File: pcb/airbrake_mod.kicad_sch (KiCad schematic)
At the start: 3 parts

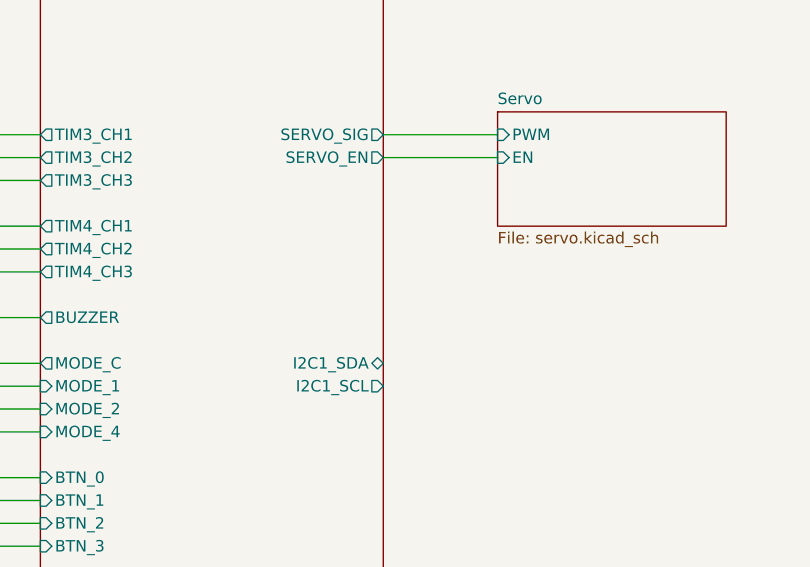
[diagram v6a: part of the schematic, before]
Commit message: Incorporate feedback servo with 4 pin molex and additional ADC channel
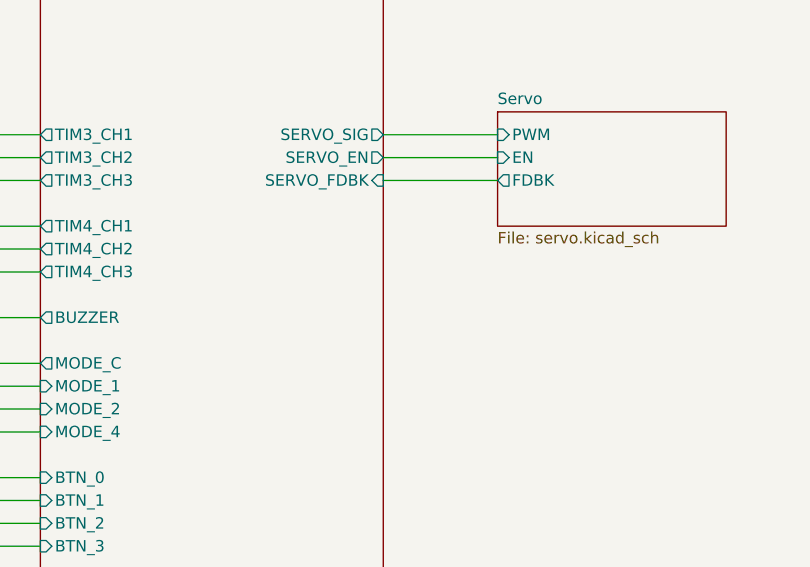
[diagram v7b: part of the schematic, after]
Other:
- sheet MCU ports: added SERVO_FDBK; removed I2C1_SCL, I2C1_SDA
- sheet Servo ports: added FDBK; removed none
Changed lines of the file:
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@@
+	(wire
+		(pts
+			(xy 101.6 121.92) (xy 114.3 121.92)
+		)
+		(stroke
+			(width 0)
+			(type default)
+		)
+	)
 	(wire
 		(pts
@@
 			)
 		)
-		(pin "I2C1_SDA" bidirectional
-			(at 101.6 142.24 0)
-			(effects
-				(font
-					(size 1.27 1.27)
-				)
-				(justify right)
-			)
-		)
-		(pin "I2C1_SCL" output
-			(at 101.6 144.78 0)
-			(effects
-				(font
-					(size 1.27 1.27)
-				)
-				(justify right)
-			)
-		)
 		(pin "USB_D-" bidirectional
 			(at 63.5 30.48 180)
@@
 				)
 				(justify left)
+			)
+		)
+		(pin "SERVO_FDBK" input
+			(at 101.6 121.92 0)
+			(effects
+				(font
+					(size 1.27 1.27)
+				)
+				(justify right)
 			)
 		)
@@
 			(effects
 				(font
+					(size 1.27 1.27)
+				)
+				(justify left)
+			)
+		)
+		(pin "FDBK" output
+			(at 114.3 121.92 180)
+			(effects
+				(font

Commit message: Add CUR schematic sheet title block
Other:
- company: (none) -> Clarkson University Rocketry Team
- title: (none) -> Air Brakes Module
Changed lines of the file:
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@@
 	(generator_version "9.0")
 	(paper "A4")
+	(title_block
+		(title "Air Brakes Module")
+		(date "2025-11-23")
+		(company "Clarkson University Rocketry Team")
+	)
 	(no_connect
 		(at 101.6 96.52)
